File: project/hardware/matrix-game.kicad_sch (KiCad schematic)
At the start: 9 parts, among them SW1 button_center, SW2 button_left, SW3 button_down, SW4 button_right, SW5 button_up, U1 NUCLEO-F042K6, U2 MAX7219

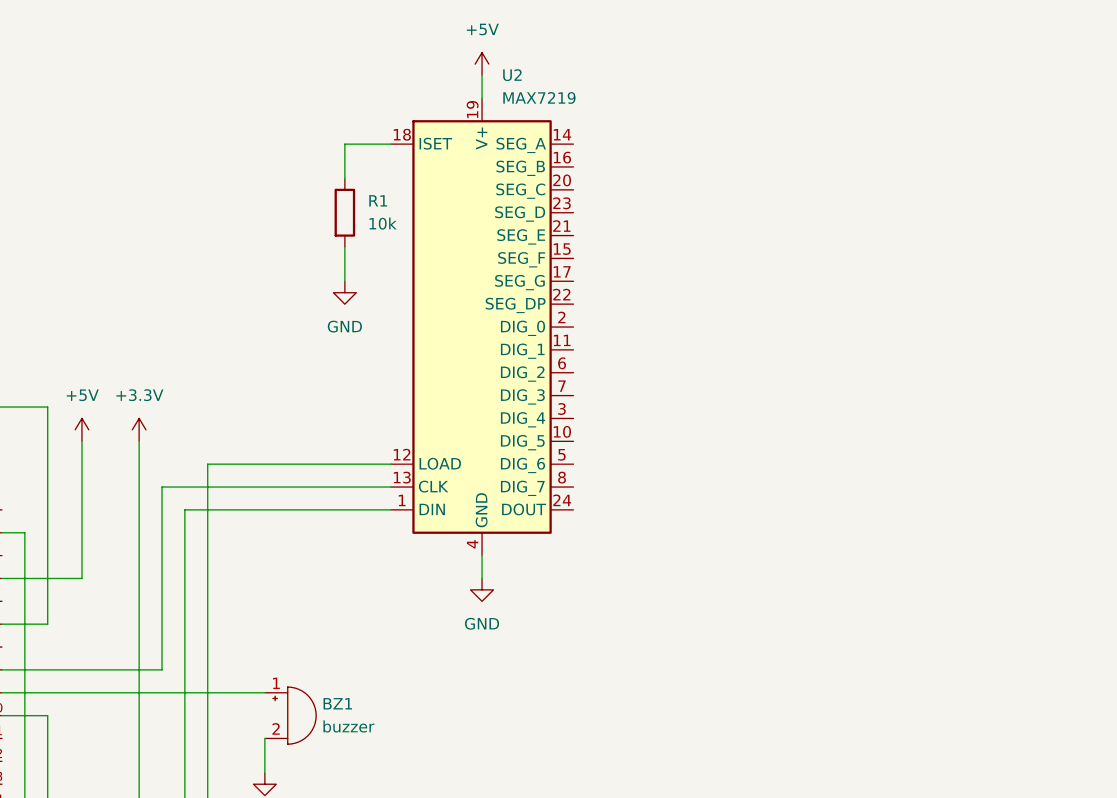
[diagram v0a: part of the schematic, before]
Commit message: [project/hardware/schematic] added max7219 and led matrix
Signed-off-by: Timon Burkard <timon.burkard@gwf.ch>
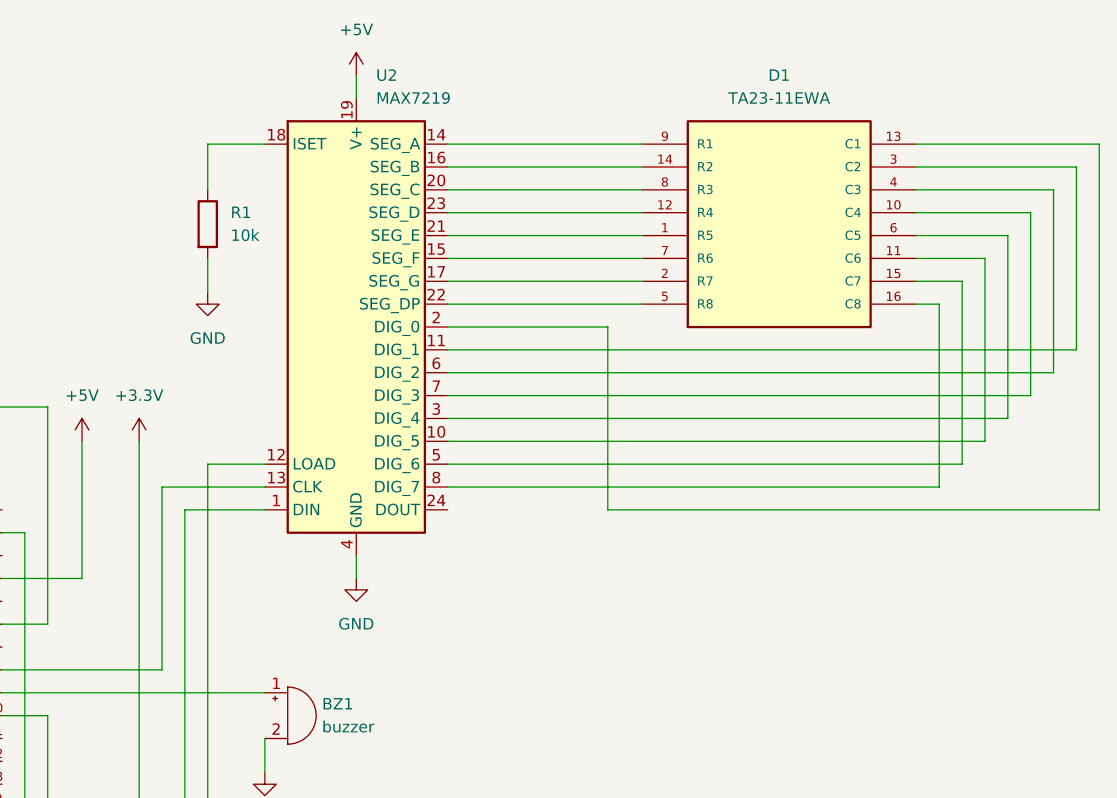
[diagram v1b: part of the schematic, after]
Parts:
- added D1: TA23-11EWA, TA23-11EWA:LED_TA23-11EWA, symbol matrix_led:TA23-11EWA
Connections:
- net at U2.10 (DIG_5): now also D1.11 (C6)
- net at U2.11 (DIG_1): now also D1.3 (C2)
- net at U2.14 (SEG_A): now also D1.9 (R1)
- net at U2.15 (SEG_F): now also D1.7 (R6)
- net at U2.16 (SEG_B): now also D1.14 (R2)
- net at U2.17 (SEG_G): now also D1.2 (R7)
- net at U2.2 (DIG_0): now also D1.13 (C1)
- net at U2.20 (SEG_C): now also D1.8 (R3)
- net at U2.21 (SEG_E): now also D1.1 (R5)
- net at U2.22 (SEG_DP): now also D1.5 (R8)
- net at U2.23 (SEG_D): now also D1.12 (R4)
- net at U2.3 (DIG_4): now also D1.6 (C5)
- net at U2.5 (DIG_6): now also D1.15 (C7)
- net at U2.6 (DIG_2): now also D1.4 (C3)
- net at U2.7 (DIG_3): now also D1.10 (C4)
- net at U2.8 (DIG_7): now also D1.16 (C8)
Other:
- moved on the sheet: R1, U2

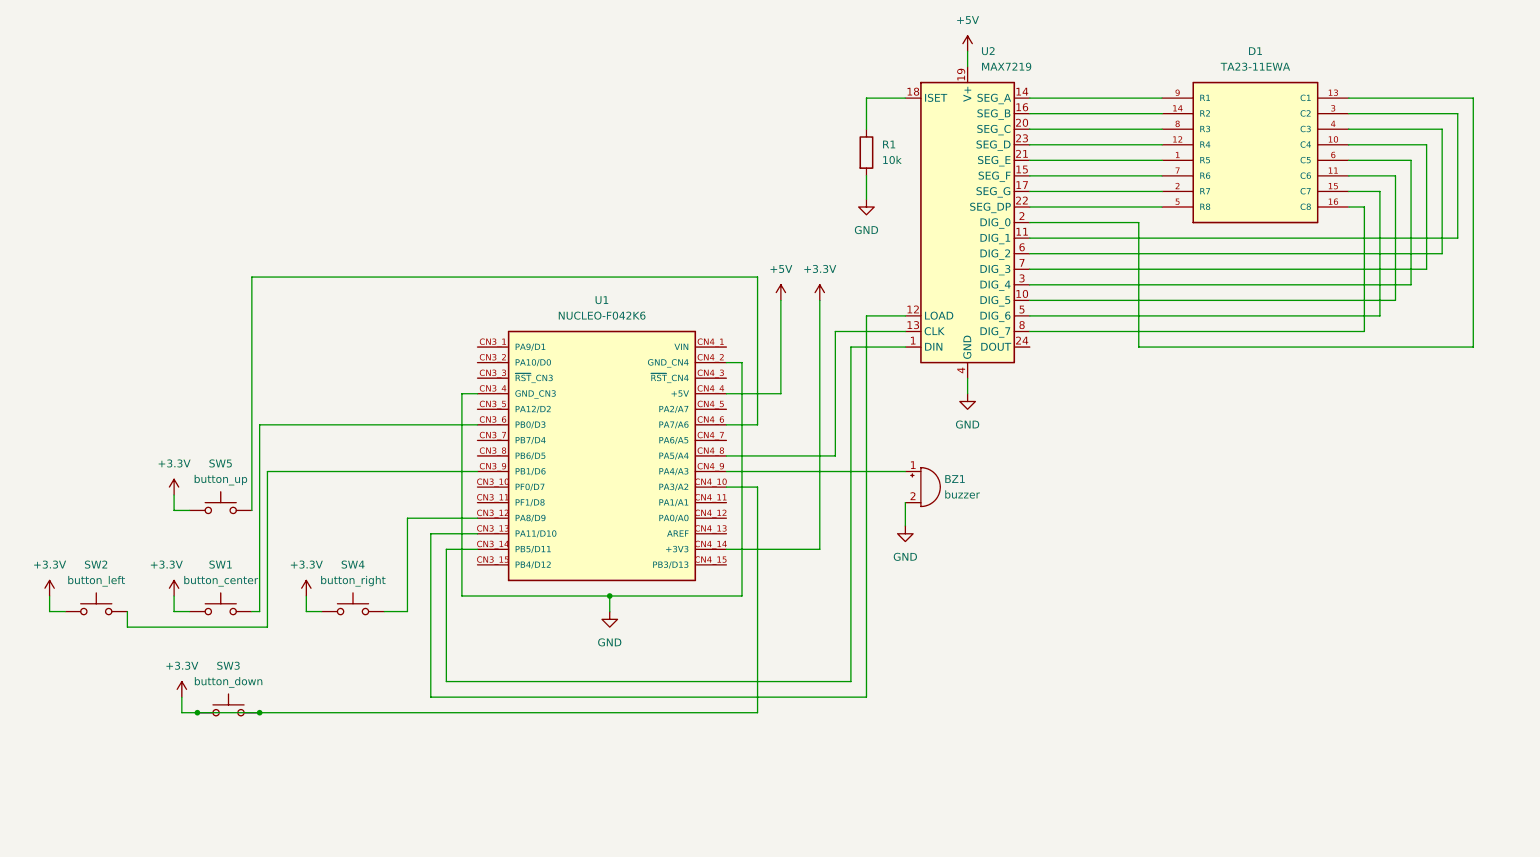
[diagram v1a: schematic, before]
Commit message: [project/hardware/schematic] added LCD
Signed-off-by: Timon Burkard <timon.burkard@gwf.ch>
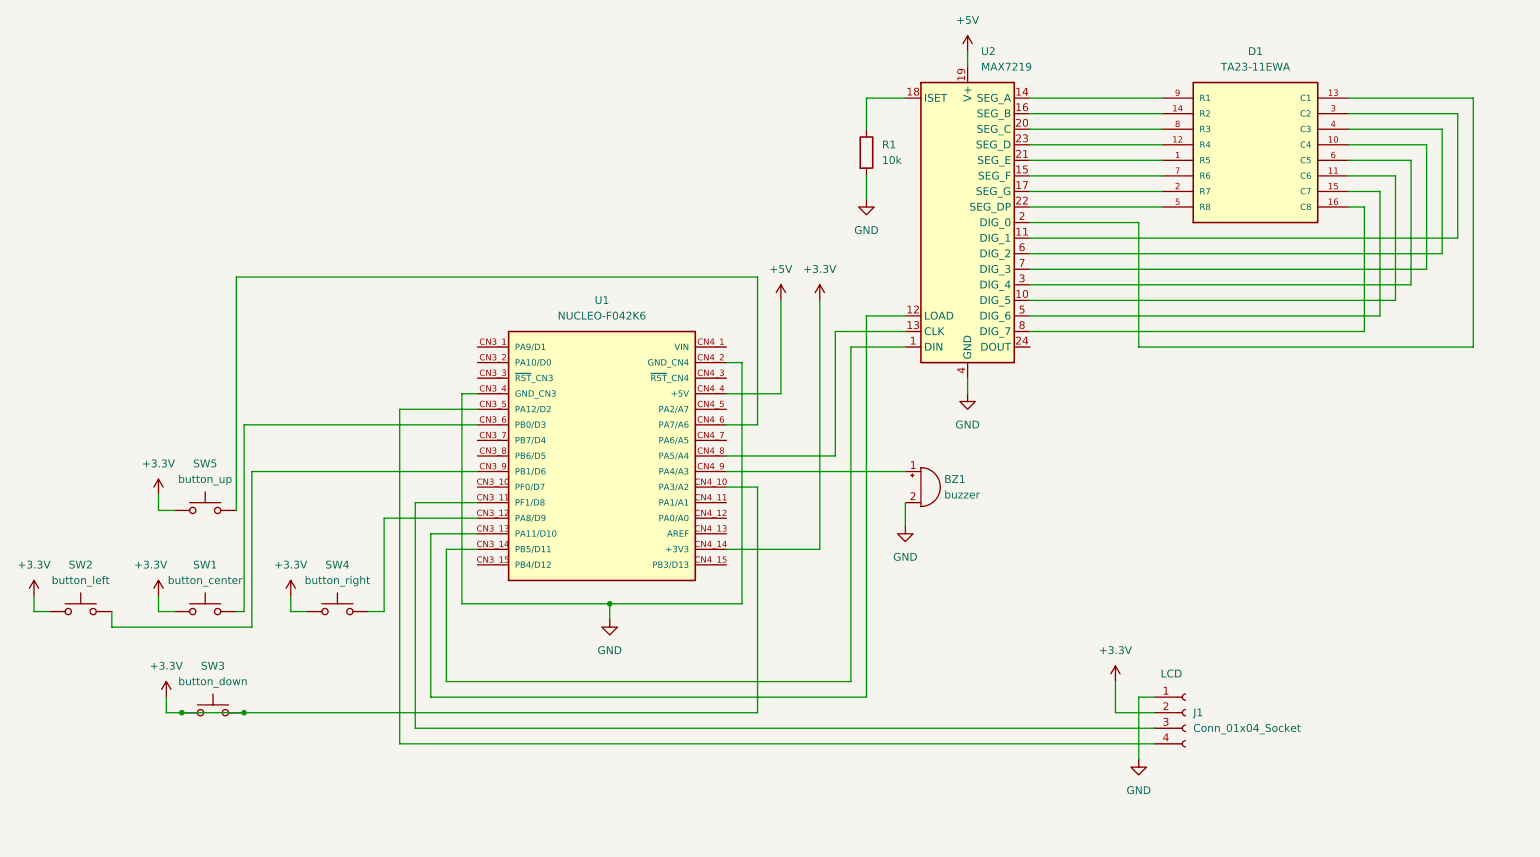
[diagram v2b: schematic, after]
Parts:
- added J1: Conn_01x04_Socket, symbol Connector:Conn_01x04_Socket
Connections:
- net +3.3V: now also J1.2 (Pin_2)
- net GND: now also J1.1 (Pin_1)
- net at U1.CN3_11 (PF1/D8): now also J1.3 (Pin_3)
- net at U1.CN3_5 (PA12/D2): now also J1.4 (Pin_4)
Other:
- note added: "LCD"
- moved on the sheet: SW1, SW2, SW3, SW4, SW5

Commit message: [project/hardware/schematic] added custom symbol for LCD, assigned footprints
Signed-off-by: Timon Burkard <timon.burkard@gwf.ch>
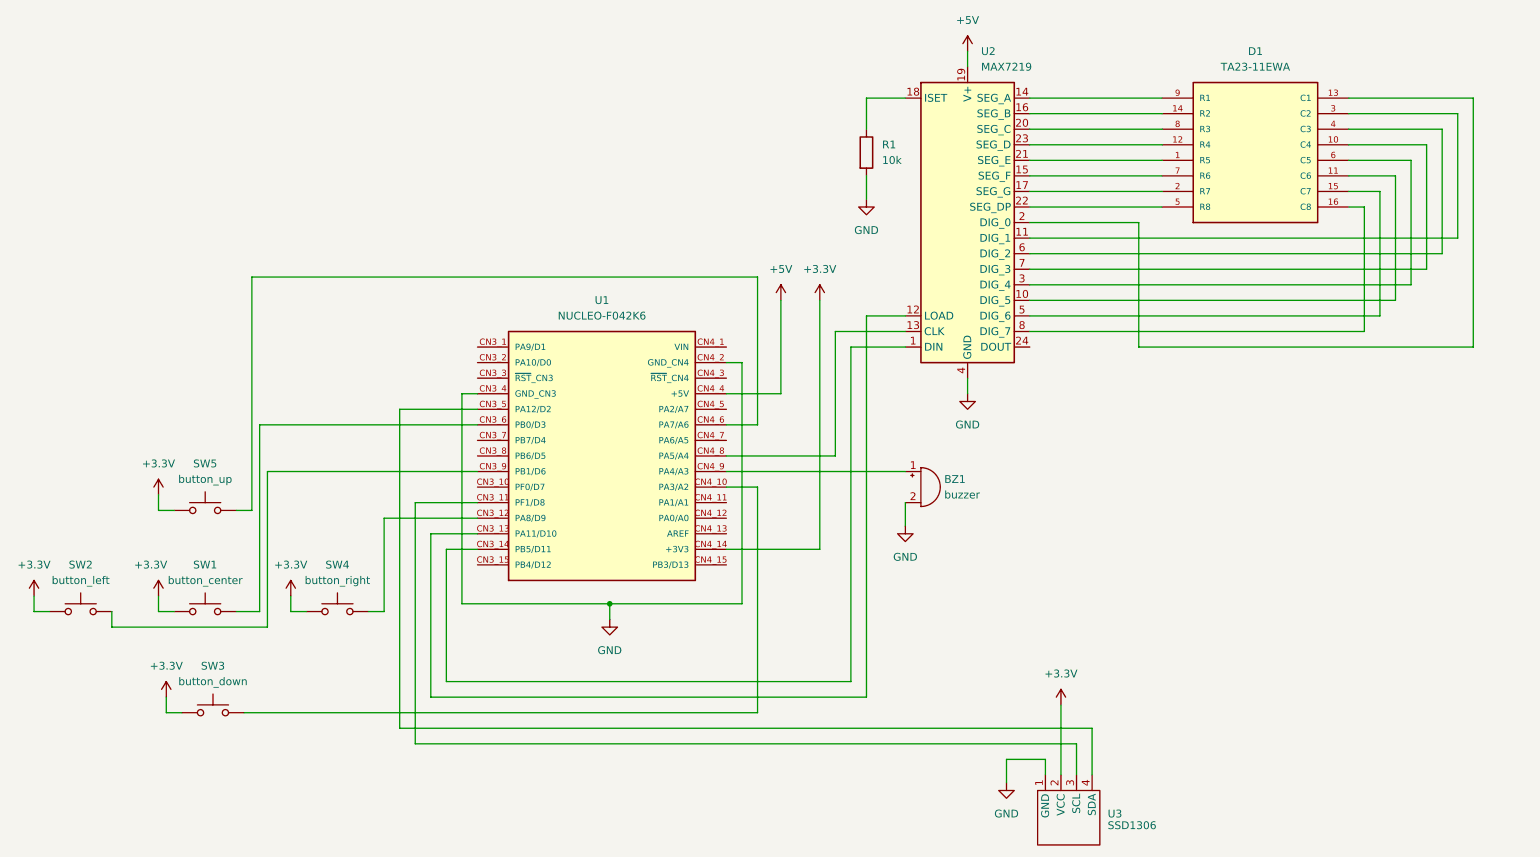
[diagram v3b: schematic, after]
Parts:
- removed J1: Conn_01x04_Socket, symbol Connector:Conn_01x04_Socket
- added U3: SSD1306, Connector_PinSocket_2.54mm:PinSocket_1x04_P2.54mm_Vertical, symbol Custom_Library:LCD_I2C
- BZ1: footprint (none) -> Buzzer_Beeper:Buzzer_12x9.5RM7.6
- D1: footprint TA23-11EWA:LED_TA23-11EWA -> matrix_led:LED_TA23-11EWA
- R1: footprint (none) -> Resistor_THT:R_Axial_DIN0207_L6.3mm_D2.5mm_P10.16mm_Horizontal
- SW1, SW2, SW3, SW4, SW5: footprint (none) -> Button_Switch_THT:SW_PUSH_6mm
- U1: footprint NUCLEO-F042K6:MODULE_NUCLEO-F042K6 -> nucleo:MODULE_NUCLEO-F042K6
- U2: footprint (none) -> Package_DIP:DIP-24_W7.62mm_Socket
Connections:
- net +3.3V: now also U3.2 (VCC); no longer SW3.2, U1.CN4_10 (PA3/A2)
- net GND: now also U3.1 (GND)
- net at U1.CN3_11 (PF1/D8): now also U3.3 (SCL)
- net at U1.CN3_5 (PA12/D2): now also U3.4 (SDA)
- new net: SW3.2, U1.CN4_10 (PA3/A2)
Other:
- note removed: "LCD"

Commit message: [project/hardware/layout] added custom footprint for LCD
Signed-off-by: Timon Burkard <timon.burkard@gwf.ch>
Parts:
- U3: footprint Connector_PinSocket_2.54mm:PinSocket_1x04_P2.54mm_Vertical -> Custom_Library:LCD_I2C
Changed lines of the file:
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@@
 			)
 		)
-		(property "Footprint" "Connector_PinSocket_2.54mm:PinSocket_1x04_P2.54mm_Vertical"
+		(property "Footprint" "Custom_Library:LCD_I2C"
 			(at 204.47 156.21 0)
 			(effects

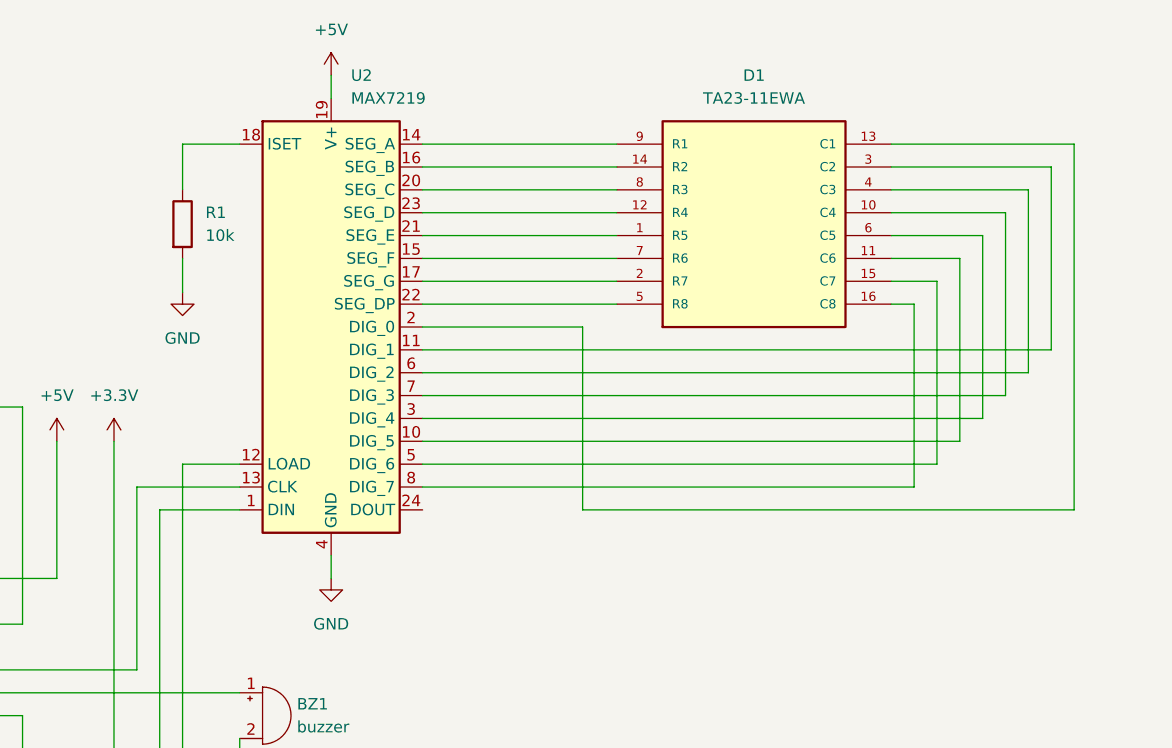
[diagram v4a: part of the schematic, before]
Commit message: [project/hardware] added test points
Signed-off-by: Timon Burkard <timon.burkard@gwf.ch>
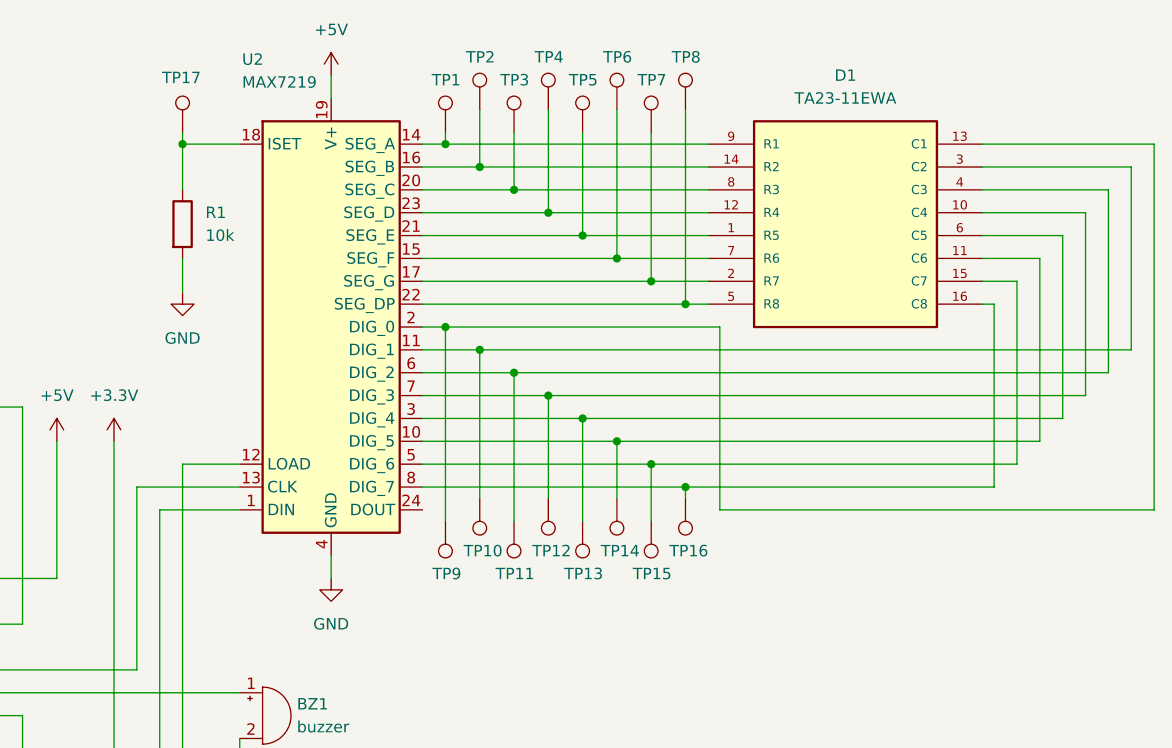
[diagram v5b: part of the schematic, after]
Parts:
- added TP1, TP10, TP11, TP12, TP13, TP14, TP15, TP16, TP17, TP2, TP3, TP4, TP5, TP6, TP7, TP8, TP9: TestPoint, Connector_PinHeader_2.54mm:PinHeader_1x01_P2.54mm_Vertical, symbol Connector:TestPoint
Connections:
- net at D1.11 (C6), U2.10 (DIG_5): now also TP14.1
- net at D1.3 (C2), U2.11 (DIG_1): now also TP10.1
- net at D1.9 (R1), U2.14 (SEG_A): now also TP1.1
- net at D1.7 (R6), U2.15 (SEG_F): now also TP6.1
- net at D1.14 (R2), U2.16 (SEG_B): now also TP2.1
- net at D1.2 (R7), U2.17 (SEG_G): now also TP7.1
- net at R1.1, U2.18 (ISET): now also TP17.1
- net at D1.13 (C1), U2.2 (DIG_0): now also TP9.1
- net at D1.8 (R3), U2.20 (SEG_C): now also TP3.1
- net at D1.1 (R5), U2.21 (SEG_E): now also TP5.1
- net at D1.5 (R8), U2.22 (SEG_DP): now also TP8.1
- net at D1.12 (R4), U2.23 (SEG_D): now also TP4.1
- net at D1.6 (C5), U2.3 (DIG_4): now also TP13.1
- net at D1.15 (C7), U2.5 (DIG_6): now also TP15.1
- net at D1.4 (C3), U2.6 (DIG_2): now also TP11.1
- net at D1.10 (C4), U2.7 (DIG_3): now also TP12.1
- net at D1.16 (C8), U2.8 (DIG_7): now also TP16.1
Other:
- moved on the sheet: D1
